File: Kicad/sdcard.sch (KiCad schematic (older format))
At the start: 4 parts, among them J301 SD_Card

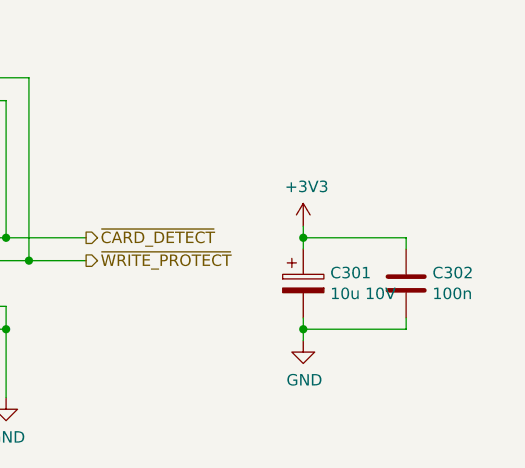
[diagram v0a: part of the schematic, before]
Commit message: Tidy-ups.
) Rewired audio block to pico
) Clarified meaning of USB power jumper and gave better
warning about not plugging in power when jumper fitted.
) We can refer to components now our sheet numbers don't change - note
Q801 on powersupply sheet
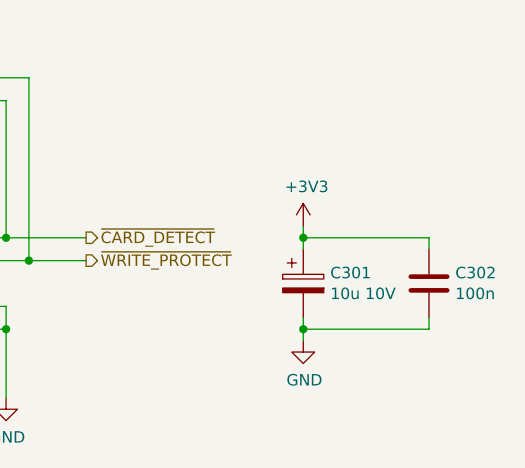
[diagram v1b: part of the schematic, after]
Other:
- moved on the sheet: C302
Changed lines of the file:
@@
 $Descr A4 11693 8268
 encoding utf-8
-Sheet 7 11
+Sheet 3 11
 Title "Neotron Common Hardware - SD Card Slot"
 Date "2021-04-17"
@@
 L Device:C C302
 U 1 1 5FE86138
-P 8700 3750
-F 0 "C302" H 8815 3796 50  0000 L CNN
-F 1 "100n" H 8815 3705 50  0000 L CNN
-F 2 "Capacitor_SMD:C_0805_2012Metric_Pad1.18x1.45mm_HandSolder" H 8738 3600 50  0001 C CNN
-F 3 "~" H 8700 3750 50  0001 C CNN
-F 4 "0" H 8700 3750 50  0001 C CNN "DNP"
-F 5 "BC1150CT-ND" H 8700 3750 50  0001 C CNN "Digikey"
-F 6 "K104K15X7RF5TL2" H 8700 3750 50  0001 C CNN "MPN"
-F 7 "Vishay" H 8700 3750 50  0001 C CNN "Manufacturer"
-F 8 "594-K104K15X7RF5TL2" H 8700 3750 50  0001 C CNN "Mouser"
-	1    8700 3750
+P 8800 3750
+F 0 "C302" H 8915 3796 50  0000 L CNN
+F 1 "100n" H 8915 3705 50  0000 L CNN
+F 2 "Capacitor_SMD:C_0805_2012Metric_Pad1.18x1.45mm_HandSolder" H 8838 3600 50  0001 C CNN
+F 3 "~" H 8800 3750 50  0001 C CNN
+F 4 "0" H 8800 3750 50  0001 C CNN "DNP"
+F 5 "BC1150CT-ND" H 8800 3750 50  0001 C CNN "Digikey"
+F 6 "K104K15X7RF5TL2" H 8800 3750 50  0001 C CNN "MPN"
+F 7 "Vishay" H 8800 3750 50  0001 C CNN "Manufacturer"
+F 8 "594-K104K15X7RF5TL2" H 8800 3750 50  0001 C CNN "Mouser"
+	1    8800 3750
 	1    0    0    -1
 $EndComp
@@
 	8250 3500 8250 3550
 Wire Wire Line
-	8250 3550 8700 3550
+	8250 3550 8800 3550
 Wire Wire Line
-	8700 3550 8700 3600
+	8800 3550 8800 3600
 Connection ~ 8250 3550
 Wire Wire Line
 	8250 3550 8250 3600
 Wire Wire Line
-	8700 3900 8700 3950
+	8800 3900 8800 3950
 Wire Wire Line
-	8700 3950 8250 3950
+	8800 3950 8250 3950
 Wire Wire Line
 	8250 3950 8250 3900

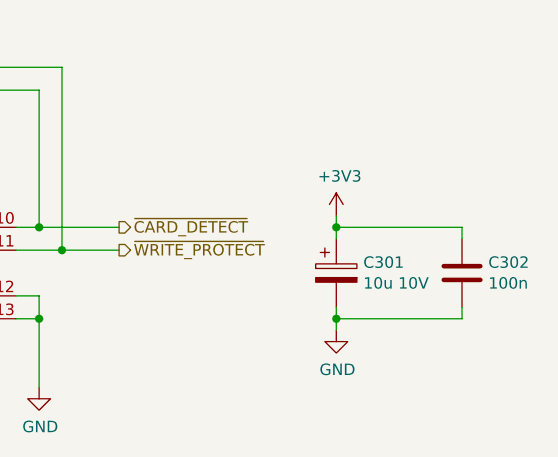
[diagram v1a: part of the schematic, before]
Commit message: Switching some parts over to the CPL.
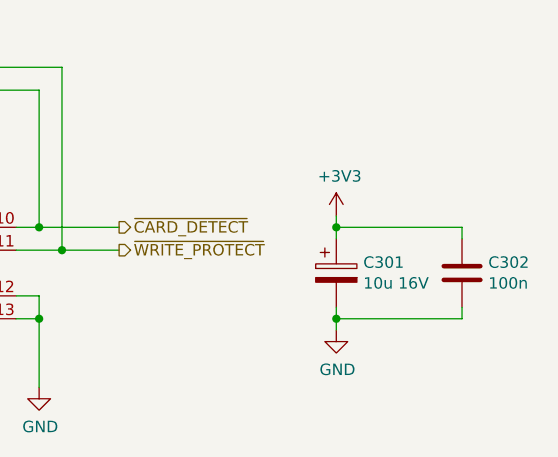
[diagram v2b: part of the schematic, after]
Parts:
- C301: value 10u 10V -> 10u 16V; Digikey 1276-6455-1-ND -> (none); MPN CL21A106KOQNNNG -> CPL-CAP-X5R-0805-10UF-16V; Manufacturer Samsung -> CPL
- C302: Digikey BC1150CT-ND -> (none); MPN K104K15X7RF5TL2 -> CPL-CAP-X7R-0805-100NF-50V; Manufacturer Vishay -> CPL; Mouser 594-K104K15X7RF5TL2 -> (none)
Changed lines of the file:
@@
 P 8250 3750
 F 0 "C301" H 8368 3796 50  0000 L CNN
-F 1 "10u 10V" H 8368 3705 50  0000 L CNN
+F 1 "10u 16V" H 8368 3705 50  0000 L CNN
 F 2 "Capacitor_SMD:C_0805_2012Metric_Pad1.18x1.45mm_HandSolder" H 8288 3600 50  0001 C CNN
 F 3 "~" H 8250 3750 50  0001 C CNN
 F 4 "0" H 8250 3750 50  0001 C CNN "DNP"
-F 5 "1276-6455-1-ND" H 8250 3750 50  0001 C CNN "Digikey"
-F 6 "CL21A106KOQNNNG" H 8250 3750 50  0001 C CNN "MPN"
-F 7 "Samsung" H 8250 3750 50  0001 C CNN "Manufacturer"
+F 5 "" H 8250 3750 50  0001 C CNN "Digikey"
+F 6 "CPL-CAP-X5R-0805-10UF-16V" H 8250 3750 50  0001 C CNN "MPN"
+F 7 "CPL" H 8250 3750 50  0001 C CNN "Manufacturer"
 	1    8250 3750
 	1    0    0    -1
@@
 F 3 "~" H 8800 3750 50  0001 C CNN
 F 4 "0" H 8800 3750 50  0001 C CNN "DNP"
-F 5 "BC1150CT-ND" H 8800 3750 50  0001 C CNN "Digikey"
-F 6 "K104K15X7RF5TL2" H 8800 3750 50  0001 C CNN "MPN"
-F 7 "Vishay" H 8800 3750 50  0001 C CNN "Manufacturer"
-F 8 "594-K104K15X7RF5TL2" H 8800 3750 50  0001 C CNN "Mouser"
+F 5 "" H 8800 3750 50  0001 C CNN "Digikey"
+F 6 "CPL-CAP-X7R-0805-100NF-50V" H 8800 3750 50  0001 C CNN "MPN"
+F 7 "CPL" H 8800 3750 50  0001 C CNN "Manufacturer"
+F 8 "" H 8800 3750 50  0001 C CNN "Mouser"
 	1    8800 3750
 	1    0    0    -1

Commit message: Fixing some review comments.
* PCB has rounded corners.
* Add JLCPCB part numbers for SMT parts
* Fixed Fab layer
* Renumbered Slots
* Mounting holes do not have thermal relief

Closes #13 #12 and #10
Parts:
- C301: LCSC Part# (none) -> C15850
- C302: LCSC Part# (none) -> C49678
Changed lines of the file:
@@
 F 7 "Kyocera" H 5950 3750 50  0001 C CNN "Manufacturer"
 F 8 "581-145638009211859+" H 5950 3750 50  0001 C CNN "Mouser"
+F 9 "~" H 5950 3750 50  0001 C CNN "LCSC Part#"
 	1    5950 3750
 	1    0    0    -1
@@
 F 6 "CPL-CAP-X5R-0805-10UF-16V" H 8250 3750 50  0001 C CNN "MPN"
 F 7 "CPL" H 8250 3750 50  0001 C CNN "Manufacturer"
+F 8 "C15850" H 8250 3750 50  0001 C CNN "LCSC Part#"
 	1    8250 3750
 	1    0    0    -1
@@
 F 7 "CPL" H 8800 3750 50  0001 C CNN "Manufacturer"
 F 8 "" H 8800 3750 50  0001 C CNN "Mouser"
+F 9 "C49678" H 8800 3750 50  0001 C CNN "LCSC Part#"
 	1    8800 3750
 	1    0    0    -1
@@
 F 7 "Bourns" H 4300 2500 50  0001 C CNN "Manufacturer"
 F 8 "652-4609X-1LF-10K" H 4300 2500 50  0001 C CNN "Mouser"
+F 9 "~" H 4300 2500 50  0001 C CNN "LCSC Part#"
 	1    4300 2500
 	1    0    0    -1

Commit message: BoM and PCB fixes.
* Move tolerances and voltages out of value and into their own fields.
* Fix 5V trace for audio stage.
* Fixup docs.yml so outputs work for JLCPCB.
* Fix JLCPCB part number for 22pF caps.
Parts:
- C301: value 10u 16V -> 10uF
- C302: value 100n -> 100nF
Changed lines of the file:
@@
 P 8250 3750
 F 0 "C301" H 8368 3796 50  0000 L CNN
-F 1 "10u 16V" H 8368 3705 50  0000 L CNN
+F 1 "10uF" H 8368 3705 50  0000 L CNN
 F 2 "Capacitor_SMD:C_0805_2012Metric_Pad1.18x1.45mm_HandSolder" H 8288 3600 50  0001 C CNN
 F 3 "~" H 8250 3750 50  0001 C CNN
@@
 P 8800 3750
 F 0 "C302" H 8915 3796 50  0000 L CNN
-F 1 "100n" H 8915 3705 50  0000 L CNN
+F 1 "100nF" H 8915 3705 50  0000 L CNN
 F 2 "Capacitor_SMD:C_0805_2012Metric_Pad1.18x1.45mm_HandSolder" H 8838 3600 50  0001 C CNN
 F 3 "~" H 8800 3750 50  0001 C CNN
